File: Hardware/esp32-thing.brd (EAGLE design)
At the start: 25.4 x 58.9 mm, 67 parts, among them Q1 2.5A/30V, Q2 MBT3904DW1T1, U1 MCP73831, U3 AP2112K-3.3V, U4 FT231XS, U5 W25Q32FVSS, Y1 26MHz, Y2 32.768kHz

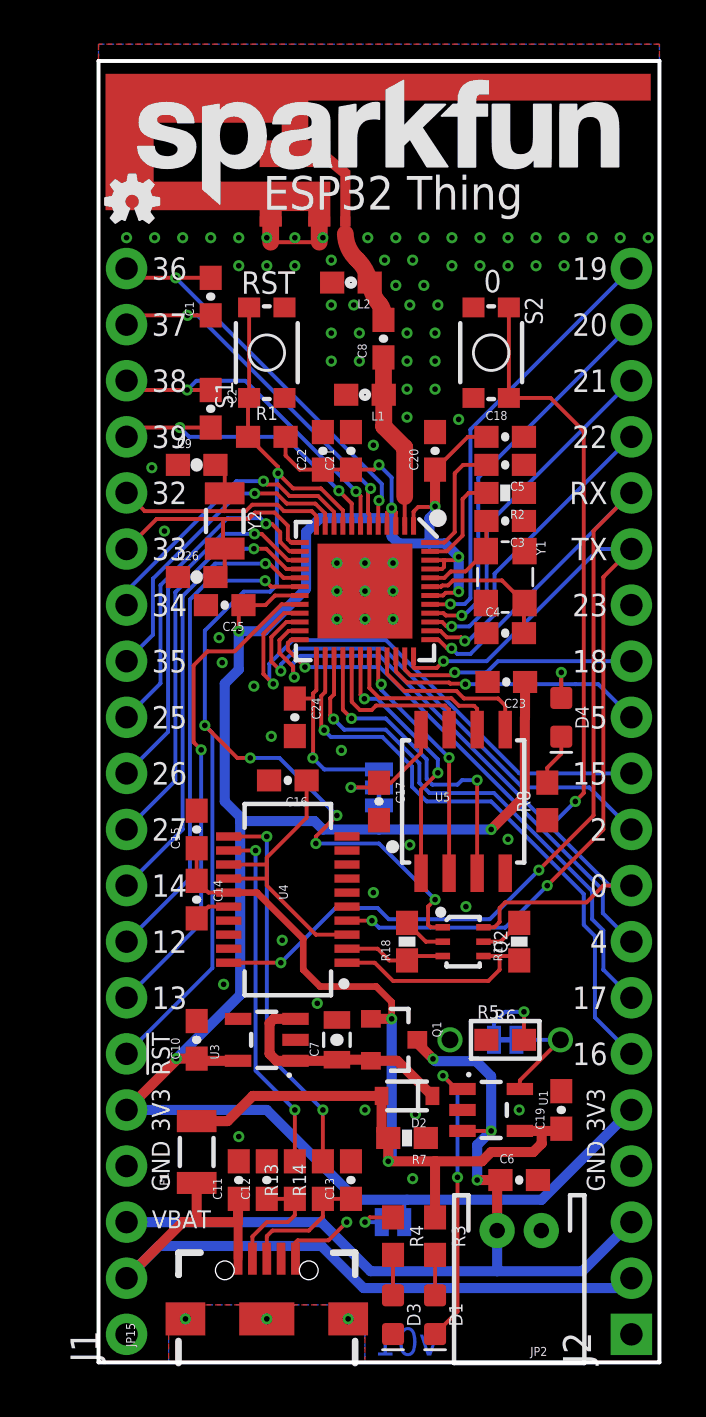
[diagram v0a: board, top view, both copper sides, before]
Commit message: Cleaning up schematic.
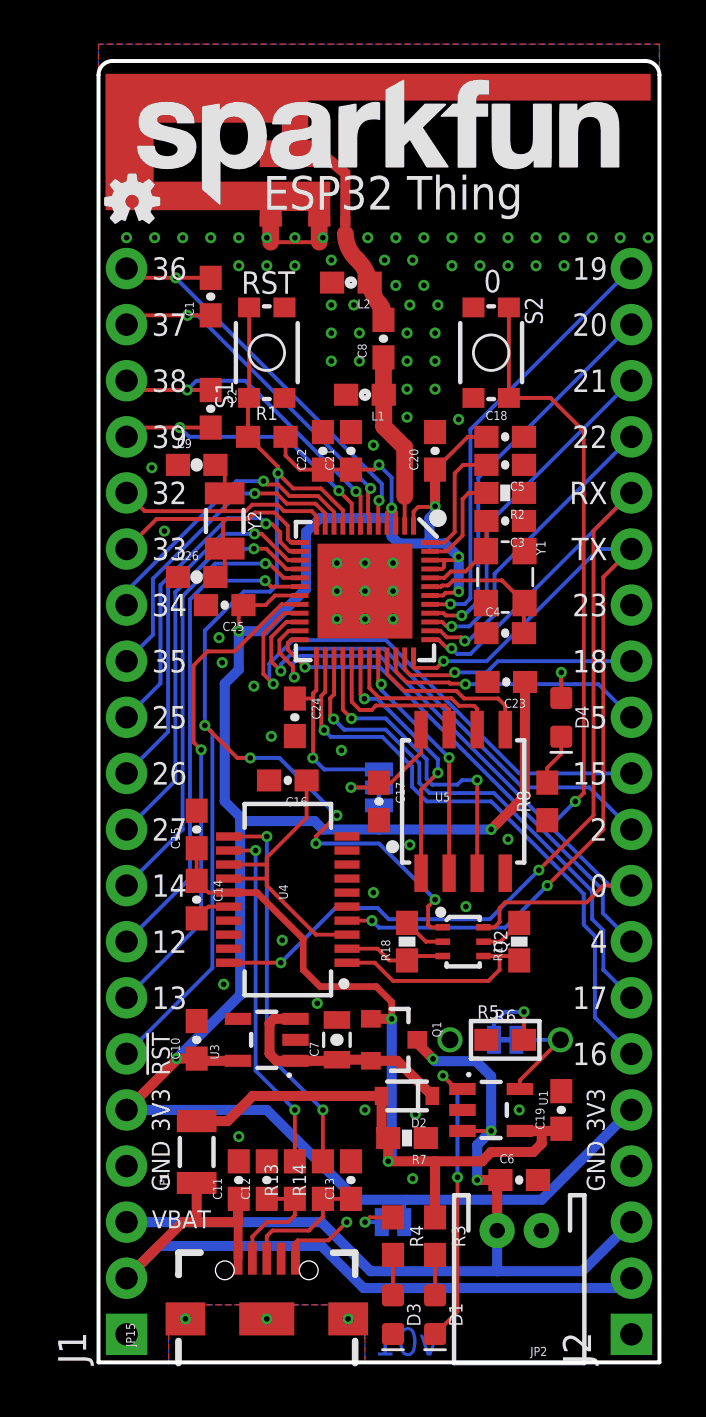
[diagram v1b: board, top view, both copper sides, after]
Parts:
- J1: device SparkFun-Connectors:1X20_NO_SILK_KIT -> SparkFun-Connectors:1X20_NOSILK
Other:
- outline, holes or cut-outs redrawn
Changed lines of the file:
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@@
 <board>
 <plain>
-<wire x1="0" y1="0" x2="0" y2="58.928" width="0.1778" layer="20"/>
-<wire x1="0" y1="58.928" x2="25.4" y2="58.928" width="0.1778" layer="20"/>
-<wire x1="25.4" y1="58.928" x2="25.4" y2="0" width="0.1778" layer="20"/>
+<wire x1="0" y1="0" x2="0" y2="58.293" width="0.1778" layer="20"/>
+<wire x1="0" y1="58.293" x2="0.635" y2="58.928" width="0.1778" layer="20" curve="-90"/>
+<wire x1="0.635" y1="58.928" x2="24.765" y2="58.928" width="0.1778" layer="20"/>
+<wire x1="24.765" y1="58.928" x2="25.4" y2="58.293" width="0.1778" layer="20" curve="-90"/>
+<wire x1="25.4" y1="58.293" x2="25.4" y2="0" width="0.1778" layer="20"/>
 <wire x1="25.4" y1="0" x2="0" y2="0" width="0.1778" layer="20"/>
 <text x="2.286" y="49.53" size="1.016" layer="22" font="vector" ratio="15" rot="MR0" align="center-right">36</text>
@@
 <element name="C9" library="SparkFun-Passives" package="0603-CAP" value="" x="4.445" y="40.64"/>
 <element name="C26" library="SparkFun-Passives" package="0603-CAP" value="" x="4.445" y="35.56"/>
-<element name="J1" library="SparkFun-Connectors" package="1X20_NO_SILK_KIT" value="" x="1.27" y="1.27" rot="R90"/>
+<element name="J1" library="SparkFun-Connectors" package="1X20_NOSILK" value="" x="1.27" y="1.27" rot="R90"/>
 <element name="J2" library="SparkFun-Connectors" package="1X20_NOSILK" value="" x="24.13" y="1.27" rot="R90"/>
 <element name="S2" library="SparkFun-Electromechanical" package="TACTILE_SWITCH_SMD_4.6X2.8MM" value="BTN-0" x="17.78" y="45.72" rot="R270">

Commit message: Adding PROD_IDs to new parts, adding new parts to temp library.
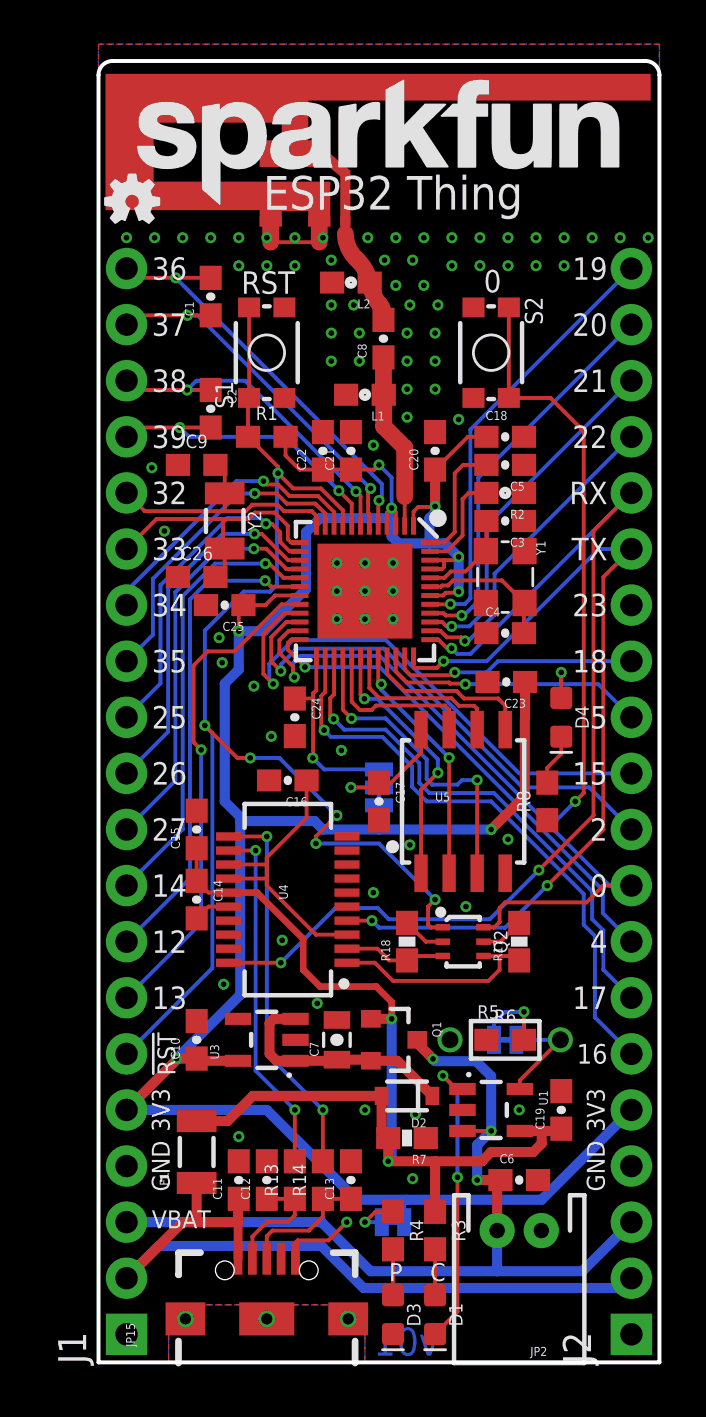
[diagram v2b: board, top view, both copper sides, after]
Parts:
- C1, C2: device SparkFun-Capacitors:0603-CAP -> esp32-thing-temp:0603-CAP
- C26, C9: value (none) -> 15pF; device SparkFun-Passives:0603-CAP -> SparkFun-Capacitors:0603
- R2: device SparkFun-Passives:0603-RES -> esp32-thing-temp:0603
- U2: value (none) -> ESP31
- moved R3 0.25 mm to (15.2, 5.97)
- moved R4 0.25 mm to (13.3, 5.97)
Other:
- board text added: "C"
- board text added: "P"

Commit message: Misc changes after running through checklist.
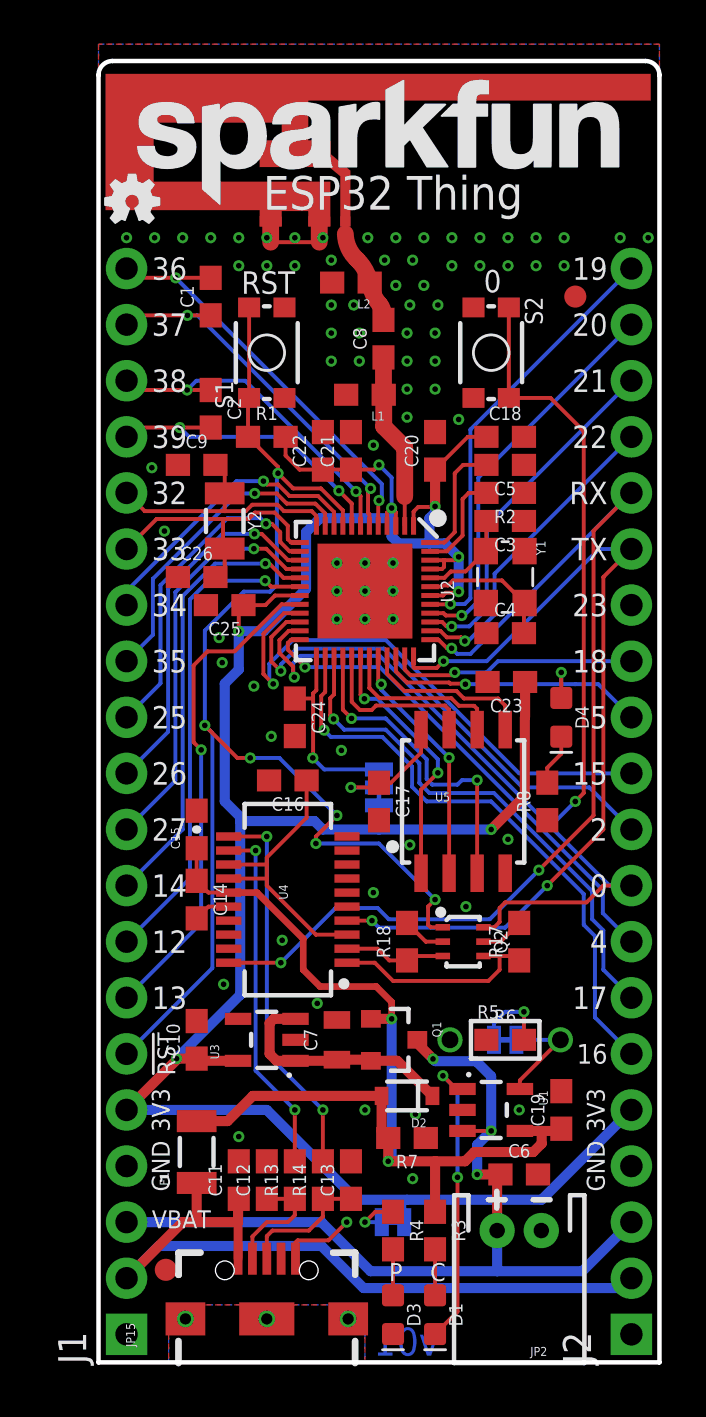
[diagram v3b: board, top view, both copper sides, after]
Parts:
- added FD1, FD2: FIDUCIAL1X2, SparkFun-Aesthetics:FIDUCIAL-1X2
- added LOGO3: SFE_LOGO_NAME.1_INCH, SparkFun-Aesthetics:SFE_LOGO_NAME_.1
- C1, C2: value 270pF -> 270PF-50V-5%(0603); device esp32-thing-temp:0603-CAP -> esp32-thing-temp:0603
- C10, C11, C12, C13, C14, C16, C17, C18, C19, C20, C21, C22, C23, C24, C25, C3, C4, C5, C6: device SparkFun-Capacitors:0603-CAP -> SparkFun-Capacitors:0603
- C7: device SparkFun-Capacitors:0805-CAP -> SparkFun-Capacitors:0805
- C8: device SparkFun-Capacitors:0603-CAP -> esp32-thing-temp:0603
- R17, R18, R7: value 10K -> 10k; device SparkFun-Resistors:0603-RES@1 -> SparkFun-Resistors:0603
- moved C6 0.25 mm to (19.1, 8.51)
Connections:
- net VUSB renamed VUSB-RAW
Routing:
- net GND: vias 78 -> 77
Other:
- board text added: "FLASH VCC"
- board text added: "http://sfe.io/t507"

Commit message: Adding name, value to C1, C2. Updating IC value.
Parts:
- C1, C2: value 270PF-50V-5%(0603) -> 270pF
- U2: value ESP31 -> ESP31B
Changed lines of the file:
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@@
 <grid distance="0.05" unitdist="inch" unit="inch" style="lines" multiple="1" display="yes" altdistance="0.005" altunitdist="inch" altunit="inch"/>
 <layers>
-<layer number="1" name="Top" color="4" fill="1" visible="no" active="yes"/>
+<layer number="1" name="Top" color="4" fill="1" visible="yes" active="yes"/>
 <layer number="2" name="Route2" color="1" fill="3" visible="no" active="no"/>
 <layer number="3" name="Route3" color="4" fill="3" visible="no" active="no"/>
@@
 <layer number="19" name="Unrouted" color="6" fill="1" visible="yes" active="yes"/>
 <layer number="20" name="Dimension" color="15" fill="1" visible="yes" active="yes"/>
-<layer number="21" name="tPlace" color="16" fill="1" visible="no" active="yes"/>
+<layer number="21" name="tPlace" color="16" fill="1" visible="yes" active="yes"/>
 <layer number="22" name="bPlace" color="14" fill="1" visible="yes" active="yes"/>
-<layer number="23" name="tOrigins" color="15" fill="1" visible="no" active="yes"/>
+<layer number="23" name="tOrigins" color="15" fill="1" visible="yes" active="yes"/>
 <layer number="24" name="bOrigins" color="15" fill="1" visible="yes" active="yes"/>
 <layer number="25" name="tNames" color="7" fill="1" visible="no" active="yes"/>
@@
 <layer number="28" name="bValues" color="7" fill="1" visible="no" active="yes"/>
 <layer number="29" name="tStop" color="7" fill="3" visible="no" active="yes"/>
-<layer number="30" name="bStop" color="7" fill="6" visible="yes" active="yes"/>
+<layer number="30" name="bStop" color="7" fill="6" visible="no" active="yes"/>
 <layer number="31" name="tCream" color="7" fill="4" visible="no" active="yes"/>
 <layer number="32" name="bCream" color="7" fill="5" visible="no" active="yes"/>
@@
 <layer number="47" name="Measures" color="7" fill="1" visible="no" active="yes"/>
 <layer number="48" name="Document" color="7" fill="1" visible="no" active="yes"/>
-<layer number="49" name="Reference" color="7" fill="1" visible="yes" active="yes"/>
+<layer number="49" name="Reference" color="7" fill="1" visible="no" active="yes"/>
 <layer number="50" name="dxf" color="7" fill="1" visible="no" active="no"/>
-<layer number="51" name="tDocu" color="6" fill="1" visible="no" active="yes"/>
-<layer number="52" name="bDocu" color="7" fill="1" visible="yes" active="yes"/>
+<layer number="51" name="tDocu" color="6" fill="1" visible="yes" active="yes"/>
+<layer number="52" name="bDocu" color="7" fill="1" visible="no" active="yes"/>
 <layer number="53" name="tGND_GNDA" color="7" fill="9" visible="no" active="no"/>
 <layer number="54" name="bGND_GNDA" color="1" fill="9" visible="no" active="no"/>
@@
 <attribute name="PROD_ID" value="CAP-11812" x="14.605" y="29.21" size="1.778" layer="27" font="vector" ratio="15" display="off"/>
 </element>
-<element name="C1" library="esp32-thing-temp" package="0603" value="270PF-50V-5%(0603)" x="5.08" y="48.26" rot="R90"/>
-<element name="C2" library="esp32-thing-temp" package="0603" value="270PF-50V-5%(0603)" x="5.08" y="43.18" rot="R270"/>
+<element name="C1" library="esp32-thing-temp" package="0603" value="270pF" x="5.08" y="48.26" rot="R90">
+<attribute name="VALUE" value="270pF" x="5.08" y="48.26" size="1.778" layer="27" rot="R90" display="off"/>
+<attribute name="PROD_ID" value="CAP-13339" x="5.08" y="48.26" size="1.778" layer="27" rot="R90" display="off"/>
+</element>
+<element name="C2" library="esp32-thing-temp" package="0603" value="270pF" x="5.08" y="43.18" rot="R270">
+<attribute name="VALUE" value="270pF" x="5.08" y="43.18" size="1.778" layer="27" rot="R270" display="off"/>
+<attribute name="PROD_ID" value="CAP-13339" x="5.08" y="43.18" size="1.778" layer="27" rot="R270" display="off"/>
+</element>
 <element name="C5" library="SparkFun-Capacitors" package="0603" value="10nF" x="18.415" y="40.64" rot="R180">
 <attribute name="PROD_ID" value="CAP-00867" x="18.415" y="40.64" size="1.778" layer="27" font="vector" ratio="15" rot="R180" display="off"/>
@@
 <attribute name="PROD_ID" value="CAP-00810" x="5.715" y="34.29" size="1.778" layer="27" font="vector" ratio="15" rot="R180" display="off"/>
 </element>
-<element name="U2" library="esp32-thing-temp" package="QFN48-0.4MM" value="ESP31" x="12.065" y="34.925" rot="R270">
+<element name="U2" library="esp32-thing-temp" package="QFN48-0.4MM" value="ESP31B" x="12.065" y="34.925" rot="R270">
 <attribute name="PROD_ID" value="IC-13338" x="12.065" y="34.925" size="1.778" layer="27" rot="R270" display="off"/>
 </element>

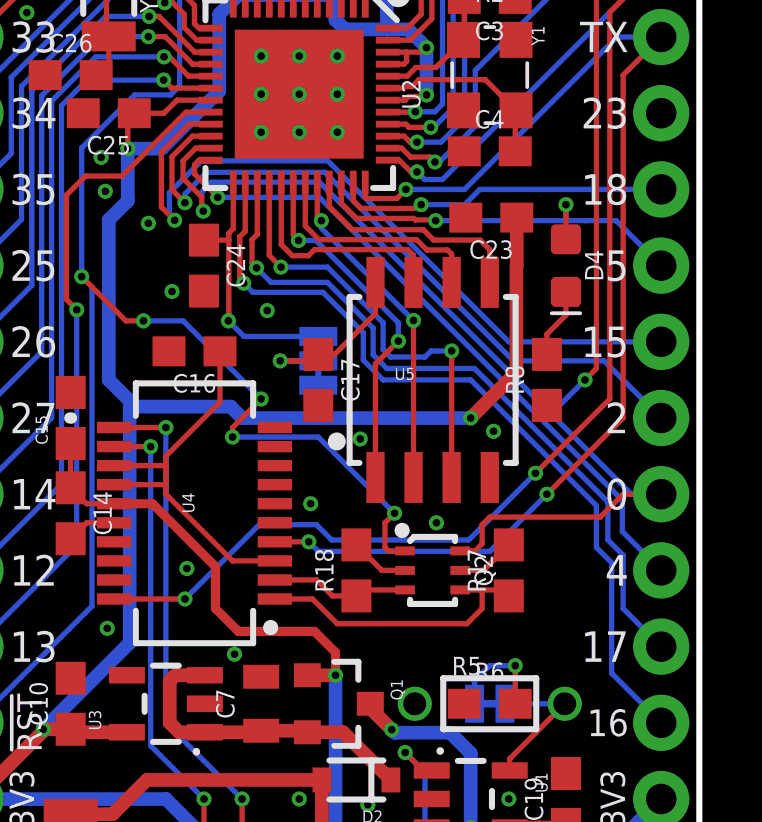
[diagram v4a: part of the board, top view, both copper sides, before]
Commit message: Fixing NPN pin assignments, flash HD and SWP pin routes.
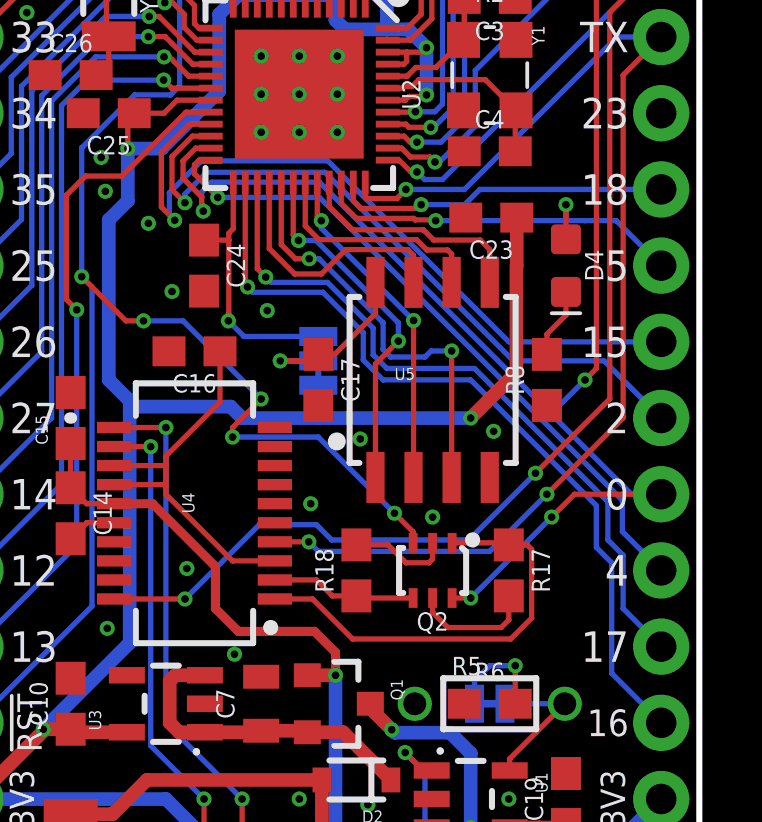
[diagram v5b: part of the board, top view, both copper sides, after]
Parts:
- turned Q2 to 180 degrees
- turned R17 to 270 degrees
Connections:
- net FLASH_SHD: now also U2.28; no longer U2.29
- net FLASH_SWP: now also U2.29; no longer U2.28
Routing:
- net DTR: track 9.78 -> 14.4 mm
- net N$10: track 1.97 -> 4.13 mm
- net N$12: track 1.97 -> 3.38 mm
- net FLASH_SHD: track 7.69 -> 8.68 mm
- net CHIP_PU: track 60.3 -> 59.6 mm
- net FLASH_SWP: track 14.7 -> 14.1 mm
- net 0: track 58.0 -> 58.5 mm, vias 2 -> 4

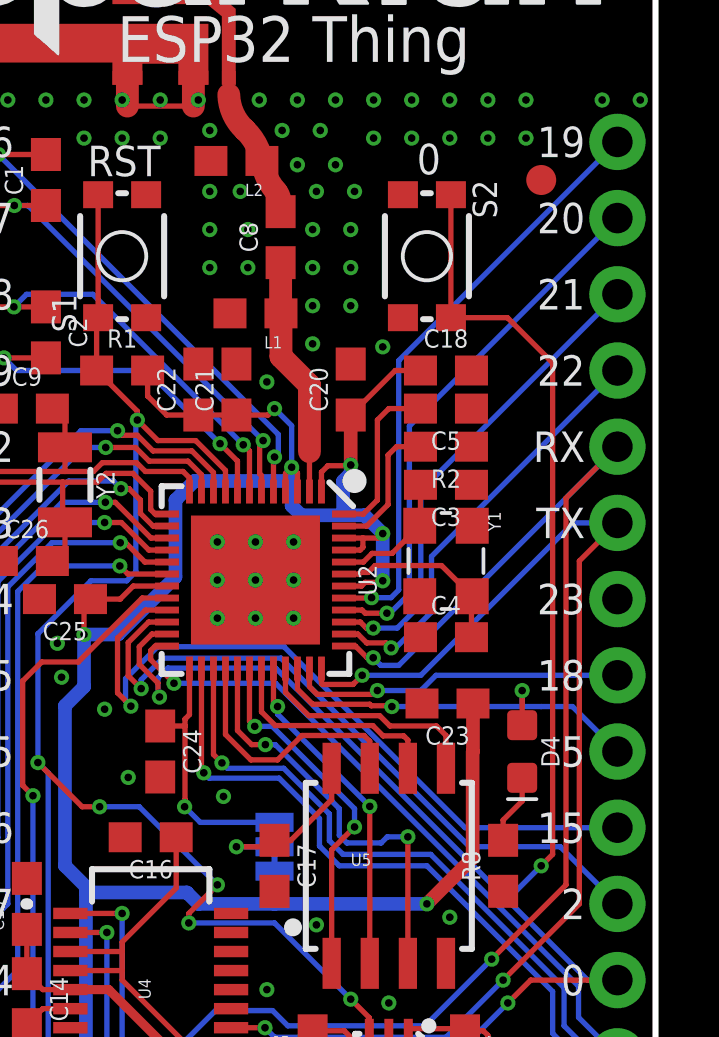
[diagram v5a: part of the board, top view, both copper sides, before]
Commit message: Added GPIO0 pullup
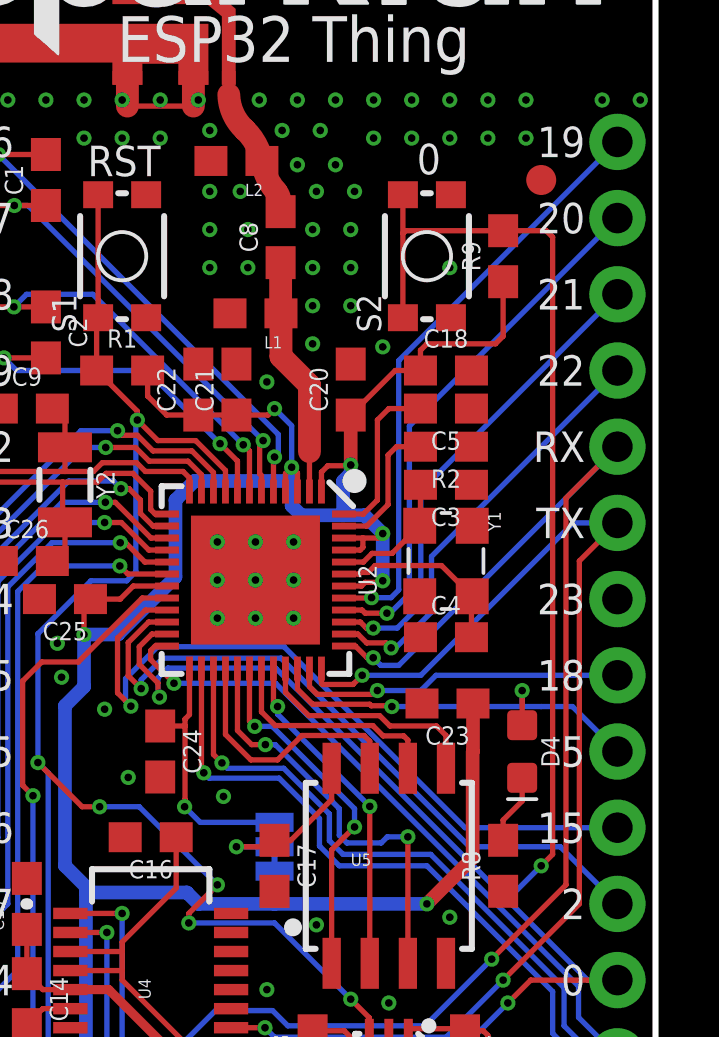
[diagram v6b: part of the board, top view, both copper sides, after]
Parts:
- added R9: 10k, SparkFun-Resistors:0603
- turned S2 to 90 degrees
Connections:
- net 0: now also R9.2
- net 3.3V: now also R9.1
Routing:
- net 3.3V: track 116.5 -> 122.0 mm
- net 0: track 58.5 -> 63.8 mm
- net GND: vias 77 -> 78
